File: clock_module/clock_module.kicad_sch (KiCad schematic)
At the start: 60 parts, among them J1 USB_C_Receptacle_PowerOnly_6P, J2 Conn_01x06_Socket, J3 Conn_01x08_Socket, SW1 SW_SPST, SW2 SW_Push, SW3 SW_SPDT, SW4 SW_SPDT, SW5 SW_DIP_x04, U1 74HC14, U10 74HC74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

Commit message: シンボル、ラベルを修正
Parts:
- removed U6, U7: 74HC153N, footprint_library:SOT38-4_NEX, symbol 74hc153:74HC153N
- added U6, U7: 74HC153, footprint_library:SOT38-4_NEX, symbol 74xx:74LS153
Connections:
- net +5V: now also U6.16 (VCC), U7.16 (VCC)
- net D5: now also U6.2 (S1), U7.2 (S1)
- net GND: now also U6.1 (Ea), U6.13 (I3b), U6.15 (Eb), U6.3 (I3a), U6.8 (GND), U7.1 (Ea), U7.13 (I3b), U7.15 (Eb), U7.3 (I3a), U7.8 (GND)
- net at R22.1, SW5.4: now also U7.12 (I2b)
- net R_A3: now reaches U2.11 (Q3)
- net R_A3: now also U7.10 (I0b)
- net R_B3: now reaches U3.11 (Q3)
- net R_B3: now also U7.11 (I1b)
- net at R21.1, SW5.3: now also U7.4 (I2a)
- net R_B2: now reaches U3.12 (Q2)
- net R_B2: now also U7.5 (I1a)
- net R_A2: now reaches U2.12 (Q2)
- net R_A2: now also U7.6 (I0a)
- net at U8.14 (A3): now also U7.7 (Za)
- net at U8.12 (A4): now also U7.9 (Zb)
- net R_A1: now reaches U2.13 (Q1)
- net R_A1: now also U6.10 (I0b)
- net R_B1: now reaches U3.13 (Q1)
- net R_B1: now also U6.11 (I1b)
- net at R20.1, SW5.2: now also U6.12 (I2b)
- net at R19.1, SW5.1: now also U6.4 (I2a)
- net R_B0: now reaches U3.14 (Q0)
- net R_B0: now also U6.5 (I1a)
- net R_A0: now reaches U2.14 (Q0)
- net R_A0: now also U6.6 (I0a)
- net at U8.5 (A1): now also U6.7 (Za)
- net at U8.3 (A2): now also U6.9 (Zb)
- net SELECT B renamed SELECT A
- net SELECT A: now also U6.14 (S0), U7.14 (S0)
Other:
- moved on the sheet: J2, J3, U10A, U1F

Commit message: 回路図からPCB更新
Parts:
- D1, D2, D3, D4: footprint (none) -> LED_THT:LED_D3.0mm
- J2: footprint (none) -> Connector_PinSocket_2.54mm:PinSocket_1x06_P2.54mm_Vertical
- J3: footprint (none) -> Connector_PinSocket_2.54mm:PinSocket_1x08_P2.54mm_Vertical
- R15, R16, R17, R18, R19, R20, R21, R22: footprint (none) -> Resistor_THT:R_Axial_DIN0207_L6.3mm_D2.5mm_P2.54mm_Vertical
- SW5: footprint (none) -> Button_Switch_THT:SW_DIP_SPSTx04_Slide_9.78x12.34mm_W7.62mm_P2.54mm
- U10: footprint (none) -> footprint_library:DIP14_TOS
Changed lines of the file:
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@@
 			)
 		)
-		(property "Footprint" ""
+		(property "Footprint" "Resistor_THT:R_Axial_DIN0207_L6.3mm_D2.5mm_P2.54mm_Vertical"
 			(at 266.7 267.208 90)
 			(effects
@@
 			)
 		)
-		(property "Footprint" ""
+		(property "Footprint" "Connector_PinSocket_2.54mm:PinSocket_1x06_P2.54mm_Vertical"
 			(at 67.31 173.99 0)
 			(effects
@@
 			)
 		)
-		(property "Footprint" ""
+		(property "Footprint" "LED_THT:LED_D3.0mm"
 			(at 251.46 274.32 0)
 			(effects
@@
 			)
 		)
-		(property "Footprint" ""
+		(property "Footprint" "LED_THT:LED_D3.0mm"
 			(at 251.46 283.21 0)
 			(effects
@@
 			)
 		)
-		(property "Footprint" ""
+		(property "Footprint" "Connector_PinSocket_2.54mm:PinSocket_1x08_P2.54mm_Vertical"
 			(at 67.31 199.39 0)
 			(effects
@@
 			)
 		)
-		(property "Footprint" ""
+		(property "Footprint" "Resistor_THT:R_Axial_DIN0207_L6.3mm_D2.5mm_P2.54mm_Vertical"
 			(at 359.41 263.398 90)
 			(effects
@@
 			)
 		)
-		(property "Footprint" ""
+		(property "Footprint" "Resistor_THT:R_Axial_DIN0207_L6.3mm_D2.5mm_P2.54mm_Vertical"
 			(at 266.7 284.988 90)
 			(effects
@@
 			)
 		)
-		(property "Footprint" ""
+		(property "Footprint" "LED_THT:LED_D3.0mm"
 			(at 251.46 265.43 0)
 			(effects
@@
 			)
 		)
-		(property "Footprint" ""
+		(property "Footprint" "Resistor_THT:R_Axial_DIN0207_L6.3mm_D2.5mm_P2.54mm_Vertical"
 			(at 266.7 293.878 90)
 			(effects
@@
 			)
 		)
-		(property "Footprint" ""
+		(property "Footprint" "footprint_library:DIP14_TOS"
 			(at 499.11 161.29 0)
 			(effects
@@
 			)
 		)
-		(property "Footprint" ""
+		(property "Footprint" "Resistor_THT:R_Axial_DIN0207_L6.3mm_D2.5mm_P2.54mm_Vertical"
 			(at 359.41 257.048 90)
 			(effects
@@
 			)
 		)
-		(property "Footprint" ""
+		(property "Footprint" "Resistor_THT:R_Axial_DIN0207_L6.3mm_D2.5mm_P2.54mm_Vertical"
 			(at 359.41 250.698 90)
 			(effects
@@
 			)
 		)
-		(property "Footprint" ""
+		(property "Footprint" "Resistor_THT:R_Axial_DIN0207_L6.3mm_D2.5mm_P2.54mm_Vertical"
 			(at 359.41 244.348 90)
 			(effects
@@
 			)
 		)
-		(property "Footprint" ""
+		(property "Footprint" "Resistor_THT:R_Axial_DIN0207_L6.3mm_D2.5mm_P2.54mm_Vertical"
 			(at 266.7 276.098 90)
 			(effects
@@
 			)
 		)
-		(property "Footprint" ""
+		(property "Footprint" "Button_Switch_THT:SW_DIP_SPSTx04_Slide_9.78x12.34mm_W7.62mm_P2.54mm"
 			(at 337.82 278.13 0)
 			(effects
@@
 			)
 		)
-		(property "Footprint" ""
+		(property "Footprint" "footprint_library:DIP14_TOS"
 			(at 64.77 251.46 0)
 			(effects
@@
 			)
 		)
-		(property "Footprint" ""
+		(property "Footprint" "LED_THT:LED_D3.0mm"
 			(at 251.46 292.1 0)
 			(effects
@@
 			)
 		)
-		(property "Footprint" ""
+		(property "Footprint" "footprint_library:DIP14_TOS"
 			(at 60.96 304.8 0)
 			(effects

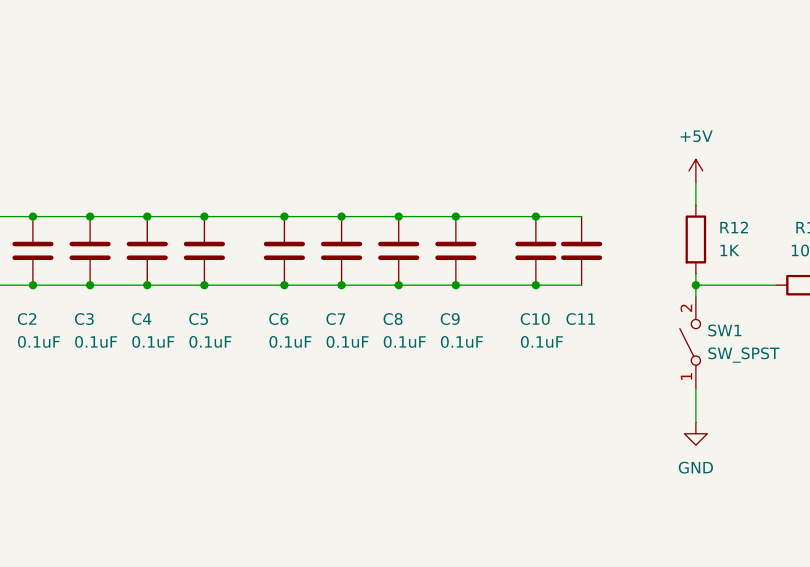
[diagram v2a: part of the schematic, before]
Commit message: コネクタを平面に変更
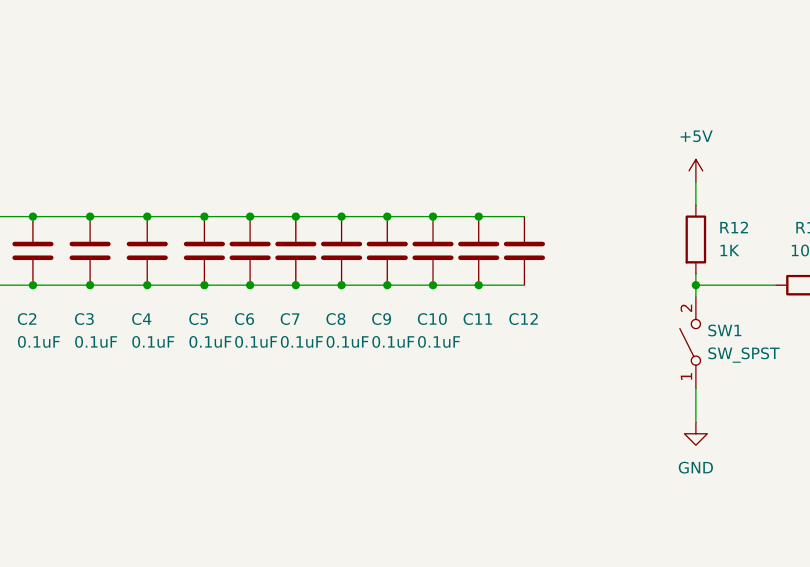
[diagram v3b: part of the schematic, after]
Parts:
- added C12: 0.1uF, Capacitor_THT:C_Disc_D4.3mm_W1.9mm_P5.00mm, symbol Device:C
- J2: footprint Connector_PinSocket_2.54mm:PinSocket_1x06_P2.54mm_Vertical -> Connector_PinSocket_2.54mm:PinSocket_1x06_P2.54mm_Horizontal
- J3: footprint Connector_PinSocket_2.54mm:PinSocket_1x08_P2.54mm_Vertical -> Connector_PinSocket_2.54mm:PinSocket_1x08_P2.54mm_Horizontal
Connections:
- net +5V: now also C12.1
- net GND: now also C12.2
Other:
- moved on the sheet: C10, C11, C6, C7, C8, C9
